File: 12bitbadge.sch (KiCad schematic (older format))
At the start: 47 parts, among them J1 Conn_02x04_Counter_Clockwise, J2 Conn_02x04_Counter_Clockwise, J3 Conn_02x04_Counter_Clockwise, J4 Conn_02x03_Odd_Even, J5 Conn_02x03_Odd_Even, J6 Conn_02x03_Odd_Even, J7 Conn_02x03_Odd_Even, Q1 Q_PMOS_GSD, Q2 Q_PMOS_GSD, Q3 Q_PMOS_GSD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

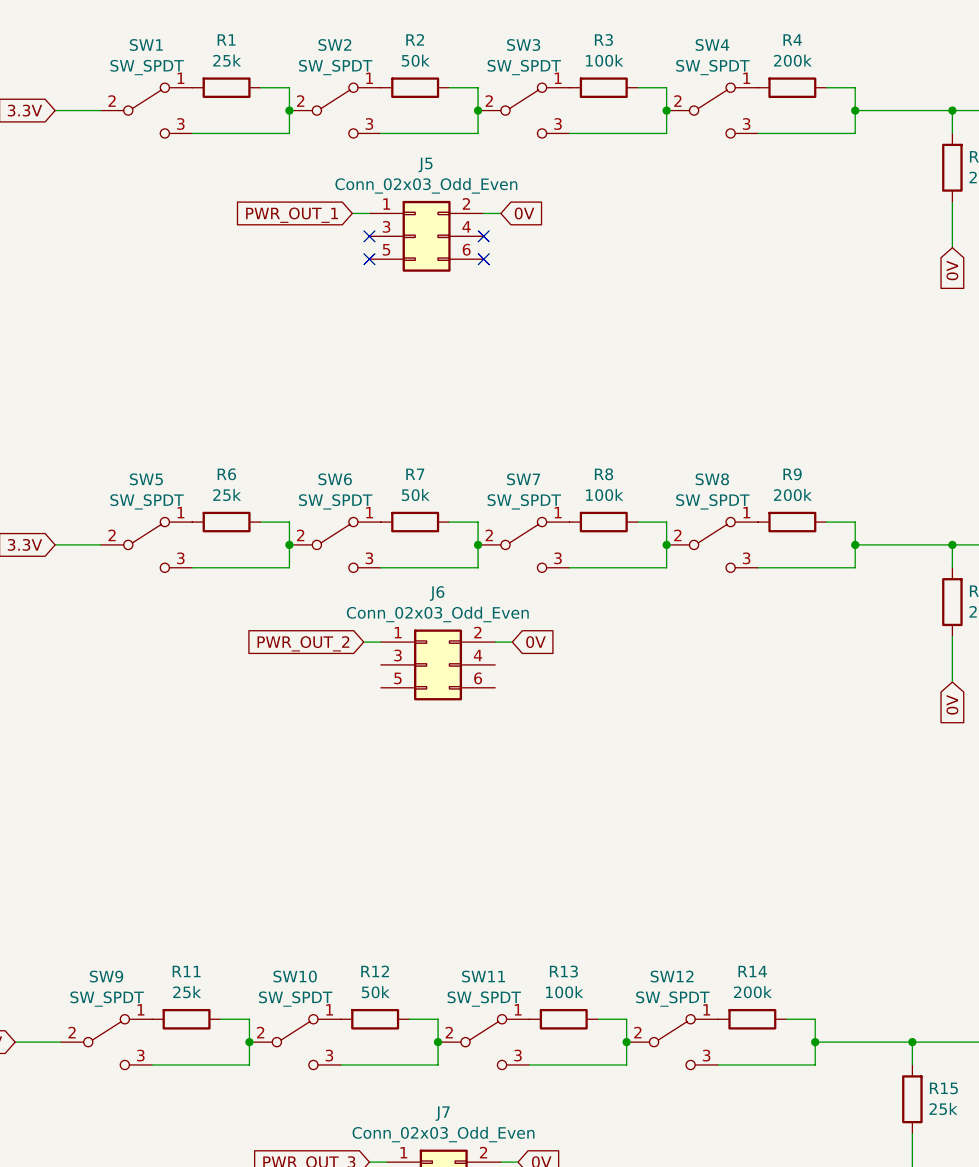
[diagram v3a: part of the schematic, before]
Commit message: Added some firmware, changed the order of the resistors to minimize ADC errors
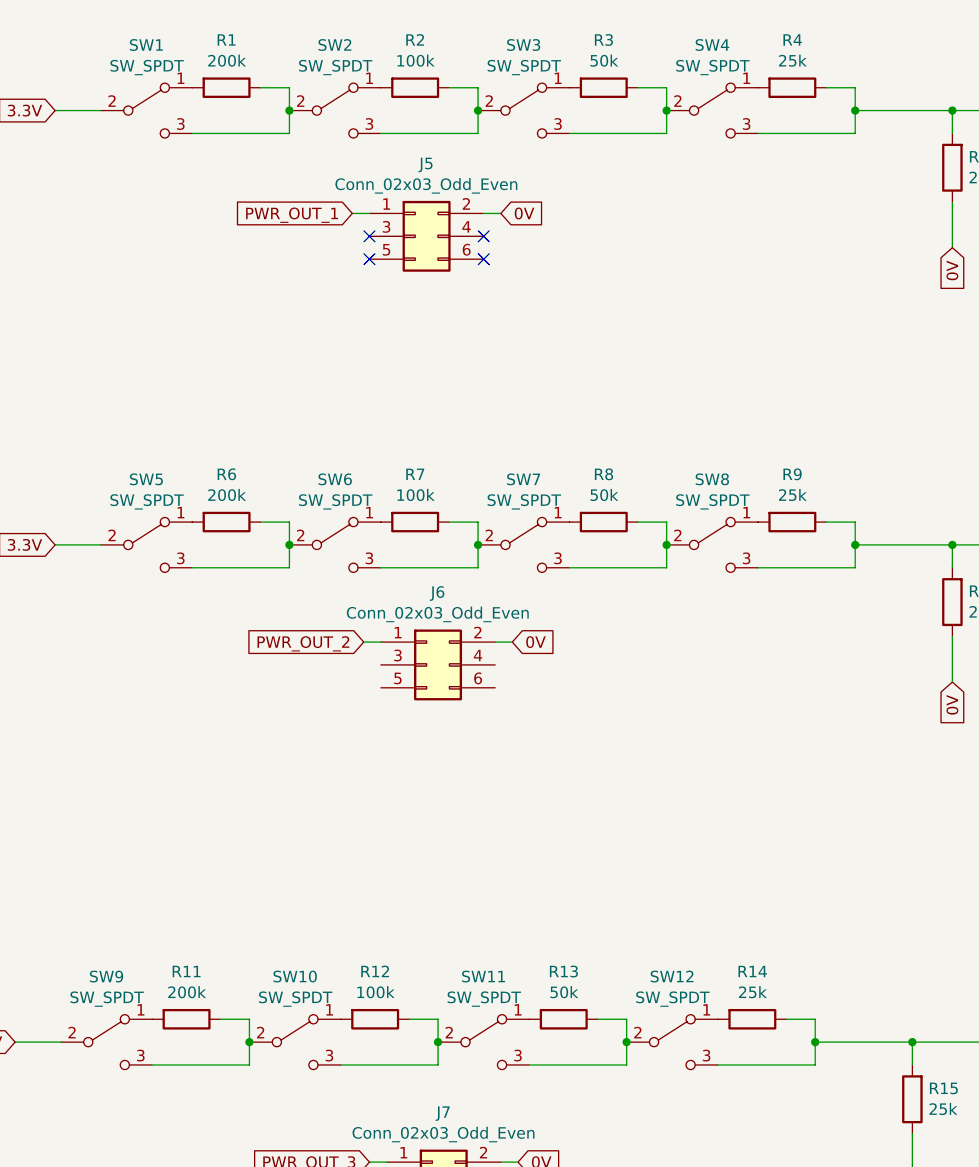
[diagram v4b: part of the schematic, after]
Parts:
- R1, R11, R6: value 25k -> 200k
- R12, R2, R7: value 50k -> 100k
- R13, R3, R8: value 100k -> 50k
- R14, R4, R9: value 200k -> 25k
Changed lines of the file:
@@
 P 6150 950
 F 0 "R2" V 5943 950 50  0000 C CNN
-F 1 "50k" V 6034 950 50  0000 C CNN
+F 1 "100k" V 6034 950 50  0000 C CNN
 F 2 "Resistor_SMD:R_0805_2012Metric_Pad1.15x1.40mm_HandSolder" V 6080 950 50  0001 C CNN
 F 3 "~" H 6150 950 50  0001 C CNN
@@
 P 6975 950
 F 0 "R3" V 6768 950 50  0000 C CNN
-F 1 "100k" V 6859 950 50  0000 C CNN
+F 1 "50k" V 6859 950 50  0000 C CNN
 F 2 "Resistor_SMD:R_0805_2012Metric_Pad1.15x1.40mm_HandSolder" V 6905 950 50  0001 C CNN
 F 3 "~" H 6975 950 50  0001 C CNN
@@
 P 7800 950
 F 0 "R4" V 7593 950 50  0000 C CNN
-F 1 "200k" V 7684 950 50  0000 C CNN
+F 1 "25k" V 7684 950 50  0000 C CNN
 F 2 "Resistor_SMD:R_0805_2012Metric_Pad1.15x1.40mm_HandSolder" V 7730 950 50  0001 C CNN
 F 3 "~" H 7800 950 50  0001 C CNN
@@
 P 5325 950
 F 0 "R1" V 5118 950 50  0000 C CNN
-F 1 "25k" V 5209 950 50  0000 C CNN
+F 1 "200k" V 5209 950 50  0000 C CNN
 F 2 "Resistor_SMD:R_0805_2012Metric_Pad1.15x1.40mm_HandSolder" V 5255 950 50  0001 C CNN
 F 3 "~" H 5325 950 50  0001 C CNN
@@
 P 6150 2850
 F 0 "R7" V 5943 2850 50  0000 C CNN
-F 1 "50k" V 6034 2850 50  0000 C CNN
+F 1 "100k" V 6034 2850 50  0000 C CNN
 F 2 "Resistor_SMD:R_0805_2012Metric_Pad1.15x1.40mm_HandSolder" V 6080 2850 50  0001 C CNN
 F 3 "~" H 6150 2850 50  0001 C CNN
@@
 P 6975 2850
 F 0 "R8" V 6768 2850 50  0000 C CNN
-F 1 "100k" V 6859 2850 50  0000 C CNN
+F 1 "50k" V 6859 2850 50  0000 C CNN
 F 2 "Resistor_SMD:R_0805_2012Metric_Pad1.15x1.40mm_HandSolder" V 6905 2850 50  0001 C CNN
 F 3 "~" H 6975 2850 50  0001 C CNN
@@
 P 7800 2850
 F 0 "R9" V 7593 2850 50  0000 C CNN
-F 1 "200k" V 7684 2850 50  0000 C CNN
+F 1 "25k" V 7684 2850 50  0000 C CNN
 F 2 "Resistor_SMD:R_0805_2012Metric_Pad1.15x1.40mm_HandSolder" V 7730 2850 50  0001 C CNN
 F 3 "~" H 7800 2850 50  0001 C CNN
@@
 P 5325 2850
 F 0 "R6" V 5118 2850 50  0000 C CNN
-F 1 "25k" V 5209 2850 50  0000 C CNN
+F 1 "200k" V 5209 2850 50  0000 C CNN
 F 2 "Resistor_SMD:R_0805_2012Metric_Pad1.15x1.40mm_HandSolder" V 5255 2850 50  0001 C CNN
 F 3 "~" H 5325 2850 50  0001 C CNN
@@
 P 5975 5025
 F 0 "R12" V 5768 5025 50  0000 C CNN
-F 1 "50k" V 5859 5025 50  0000 C CNN
+F 1 "100k" V 5859 5025 50  0000 C CNN
 F 2 "Resistor_SMD:R_0805_2012Metric_Pad1.15x1.40mm_HandSolder" V 5905 5025 50  0001 C CNN
 F 3 "~" H 5975 5025 50  0001 C CNN
@@
 P 6800 5025
 F 0 "R13" V 6593 5025 50  0000 C CNN
-F 1 "100k" V 6684 5025 50  0000 C CNN
+F 1 "50k" V 6684 5025 50  0000 C CNN
 F 2 "Resistor_SMD:R_0805_2012Metric_Pad1.15x1.40mm_HandSolder" V 6730 5025 50  0001 C CNN
 F 3 "~" H 6800 5025 50  0001 C CNN
@@
 P 7625 5025
 F 0 "R14" V 7418 5025 50  0000 C CNN
-F 1 "200k" V 7509 5025 50  0000 C CNN
+F 1 "25k" V 7509 5025 50  0000 C CNN
 F 2 "Resistor_SMD:R_0805_2012Metric_Pad1.15x1.40mm_HandSolder" V 7555 5025 50  0001 C CNN
 F 3 "~" H 7625 5025 50  0001 C CNN
@@
 P 5150 5025
 F 0 "R11" V 4943 5025 50  0000 C CNN
-F 1 "25k" V 5034 5025 50  0000 C CNN
+F 1 "200k" V 5034 5025 50  0000 C CNN
 F 2 "Resistor_SMD:R_0805_2012Metric_Pad1.15x1.40mm_HandSolder" V 5080 5025 50  0001 C CNN
 F 3 "~" H 5150 5025 50  0001 C CNN

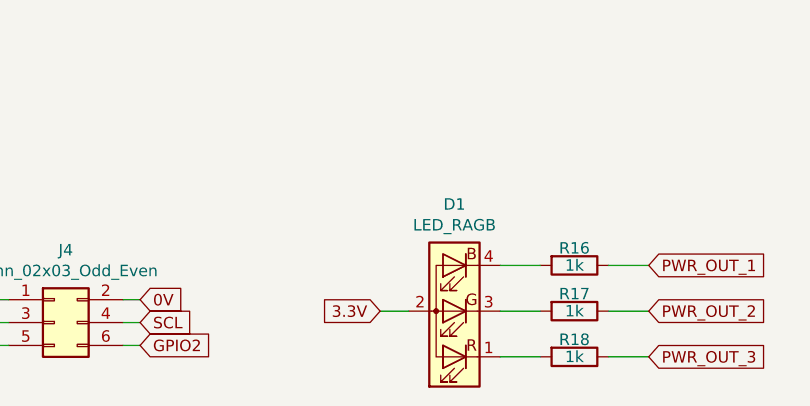
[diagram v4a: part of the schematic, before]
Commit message: Changed from common-anode RGB LED to common-cathode RGB LED
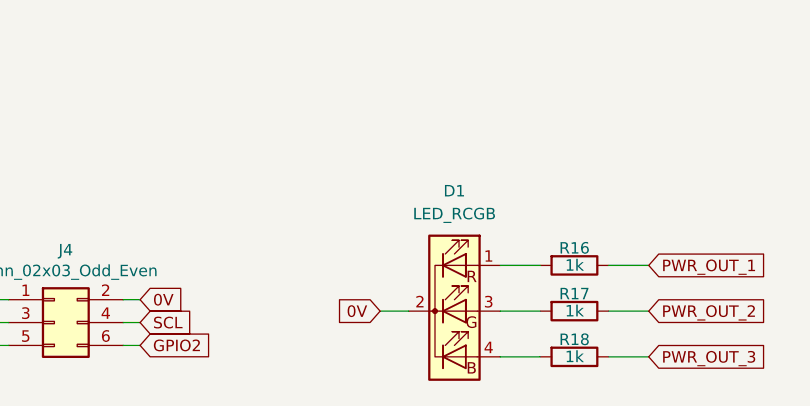
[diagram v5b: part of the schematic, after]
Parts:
- removed D1: LED_RAGB, LED_THT:LED_D5.0mm-4_RGB, symbol Device:LED_RAGB
- added D1: LED_RCGB, LED_THT:LED_D5.0mm-4_RGB, symbol Device:LED_RCGB
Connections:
- net 0V: now also D1.2 (K)
- net at R18.2: now also D1.4 (BA)
- net at R17.2: now also D1.3 (GA)
- net at R16.2: now also D1.1 (RA)
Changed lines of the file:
@@
 Wire Wire Line
 	6600 5650 6525 5650
-$Comp
-L Device:LED_RAGB D1
-U 1 1 5E3022FD
-P 3100 7325
-F 0 "D1" H 3100 6858 50  0000 C CNN
-F 1 "LED_RAGB" H 3100 6949 50  0000 C CNN
-F 2 "LED_THT:LED_D5.0mm-4_RGB" H 3100 7275 50  0001 C CNN
-F 3 "~" H 3100 7275 50  0001 C CNN
-	1    3100 7325
-	-1   0    0    1
-$EndComp
-Text GLabel 2775 7325 0    50   Input ~ 0
-3.3V
 Wire Wire Line
 	2775 7325 2900 7325
@@
 Wire Wire Line
 	10225 5050 10225 5200
+Text GLabel 2775 7325 0    50   Input ~ 0
+0V
+$Comp
+L Device:LED_RCGB D1
+U 1 1 5E65101F
+P 3100 7325
+F 0 "D1" H 3100 7850 50  0000 C CNN
+F 1 "LED_RCGB" H 3100 7750 50  0000 C CNN
+F 2 "LED_THT:LED_D5.0mm-4_RGB" H 3100 7275 50  0001 C CNN
+F 3 "~" H 3100 7275 50  0001 C CNN
+	1    3100 7325
+	1    0    0    -1
+$EndComp
 $EndSCHEMATC
